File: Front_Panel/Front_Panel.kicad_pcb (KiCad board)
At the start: 2 copper layers, 160 x 70 mm, 27 parts, among them J2 Conn_01x05, Q1 BC817, SW1 SW_Push, SW2 SW_Push, SW3 SW_Push, SW4 SW_Push, U1 NHD-C0220BIZ, U2 MCP23008-xSO

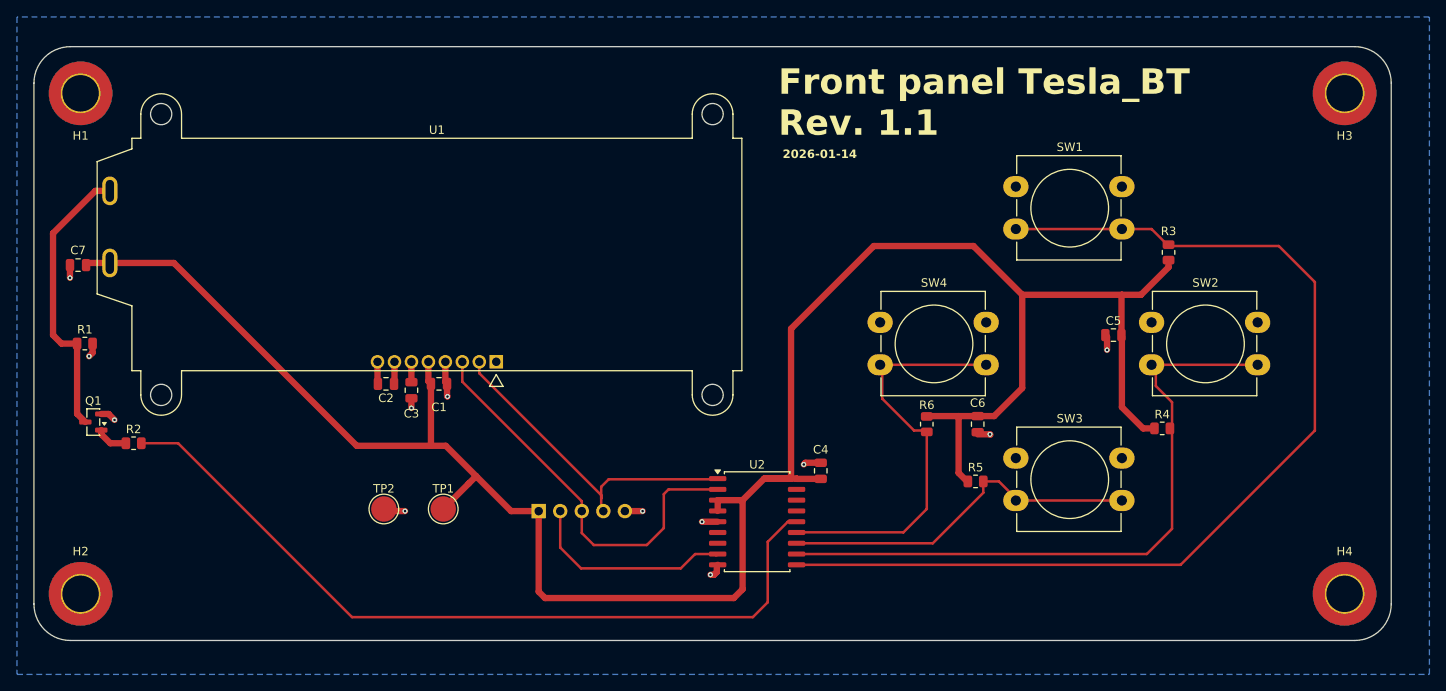
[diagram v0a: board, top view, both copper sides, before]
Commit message: changes with BOM, minor fixes
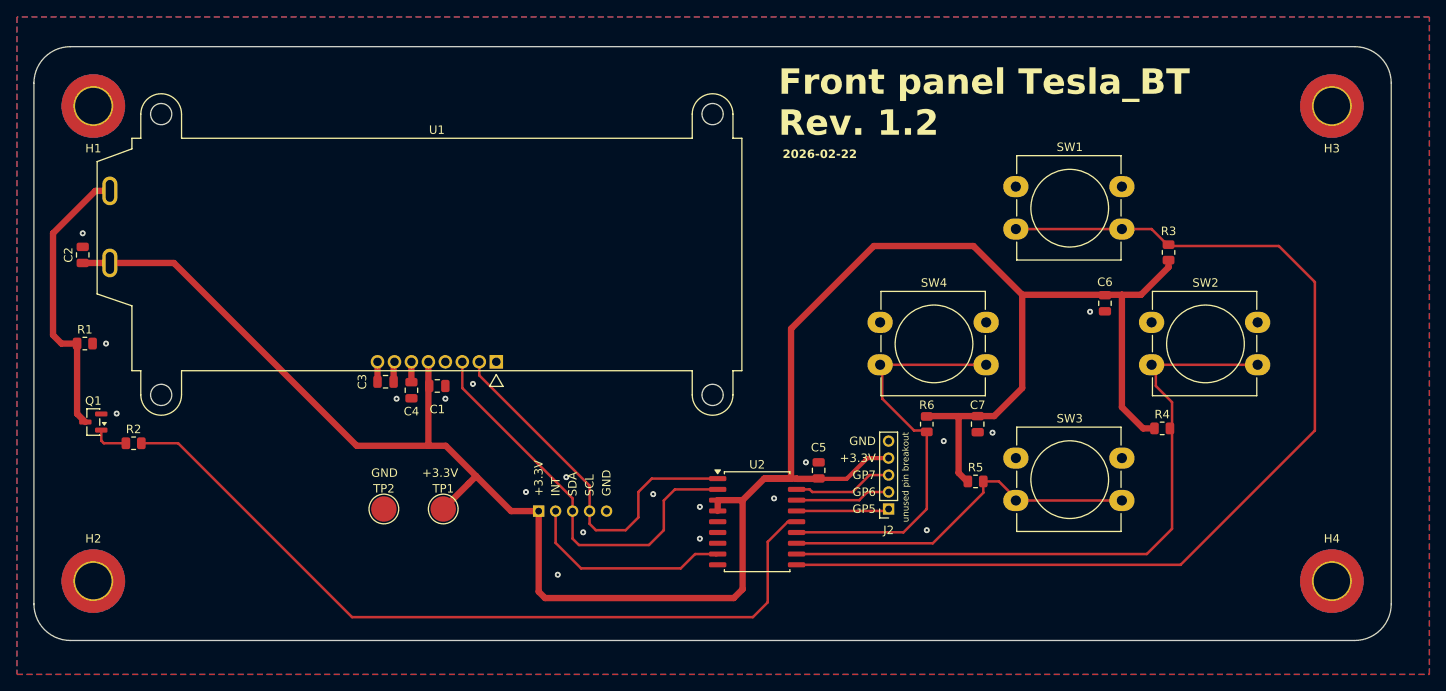
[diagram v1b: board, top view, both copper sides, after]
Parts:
- added J1: Conn_01x05, Connector_PinSocket_2.00mm:PinSocket_1x05_P2.00mm_Vertical, B.Cu at (127.5, 127.2)
- C4: value 100nF -> 470nF
- C7: value 470nF -> 100nF
- J2: footprint Connector_PinSocket_2.54mm:PinSocket_1x05_P2.54mm_Vertical -> Connector_PinSocket_2.00mm:PinSocket_1x05_P2.00mm_Vertical; moved to F.Cu
- moved C7 107.7 mm to (179.2, 117.0), turned to -90 degrees
- moved C4 49.2 mm to (112.5, 113.0), turned to -90 degrees
- moved J2 41.3 mm to (168.8, 127.0), turned to 180 degrees
- moved C2 38.8 mm to (73.8, 97.0), turned to 90 degrees
- moved C5 38.2 mm to (160.5, 122.5), turned to 90 degrees
- moved C6 20.7 mm to (194.2, 102.8), turned to 90 degrees
- moved C3 3.21 mm to (109.5, 112.0), turned to 180 degrees
- moved H1 2.12 mm to (75.0, 79.5)
- moved H2 2.12 mm to (75.0, 135.5)
- moved H3 2.12 mm to (221.0, 79.5)
- moved H4 2.12 mm to (221.0, 135.5)
- moved C1 0.32 mm to (115.5, 112.5)
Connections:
- C2 pad 1: Net-(U1-C1+) -> +3.3V
- C2 pad 2: Net-(U1-C1-) -> GND
- C3 pad 1: Net-(U1-VOUT) -> Net-(U1-C1+)
- C3 pad 2: GND -> Net-(U1-C1-)
- C4 pad 1: +3.3V -> Net-(U1-VOUT)
- C5 pad 1: GND -> +3.3V
- C5 pad 2: +3.3V -> GND
- C6 pad 1: +3.3V -> GND
- C6 pad 2: GND -> +3.3V
- J2 pad 1: +3.3V -> Net-(J2-Pin_1)
- J2 pad 2: /I2C_IO.INT -> Net-(J2-Pin_2)
- J2 pad 3: /I2C_IO.SDA -> Net-(J2-Pin_3)
- J2 pad 4: /I2C_IO.SCL -> +3.3V
- U2 pad 15: unconnected-(U2-GP5-Pad15) -> Net-(J2-Pin_1)
- U2 pad 16: unconnected-(U2-GP6-Pad16) -> Net-(J2-Pin_2)
- U2 pad 17: unconnected-(U2-GP7-Pad17) -> Net-(J2-Pin_3)
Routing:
- net GND: track 24.1 -> 0.00 mm, vias 12 -> 19
- net Net-(J2-Pin_3): track 0.00 -> 11.8 mm
- net Net-(J2-Pin_2): track 0.00 -> 11.2 mm
- net Net-(J2-Pin_1): track 0.00 -> 10.9 mm
- net +3.3V: track 264.4 -> 273.4 mm
- net /I2C_IO.SCL: track 39.5 -> 44.3 mm
- net /I2C_IO.SDA: track 47.7 -> 48.4 mm
- added copper zone on F.Cu, net GND
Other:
- board text added: "+3.3V"
- board text added: "2026-02-22"
- board text added: "Front panel Tesla_BT Rev. 1.2"
- board text added: "GND"
- board text added: "GP5"
- board text added: "GP6"
- board text added: "GP7"
- board text added: "INT"
- board text added: "SCL"
- board text added: "SDA"
- board text added: "unused pin breakout"
- board text removed: "2026-01-14"
- board text removed: "Front panel Tesla_BT Rev. 1.1"
